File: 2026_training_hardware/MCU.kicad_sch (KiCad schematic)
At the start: 2 parts, among them J1 RJ45_LED_Shielded, U1 Teensy4.1_DEV-16771

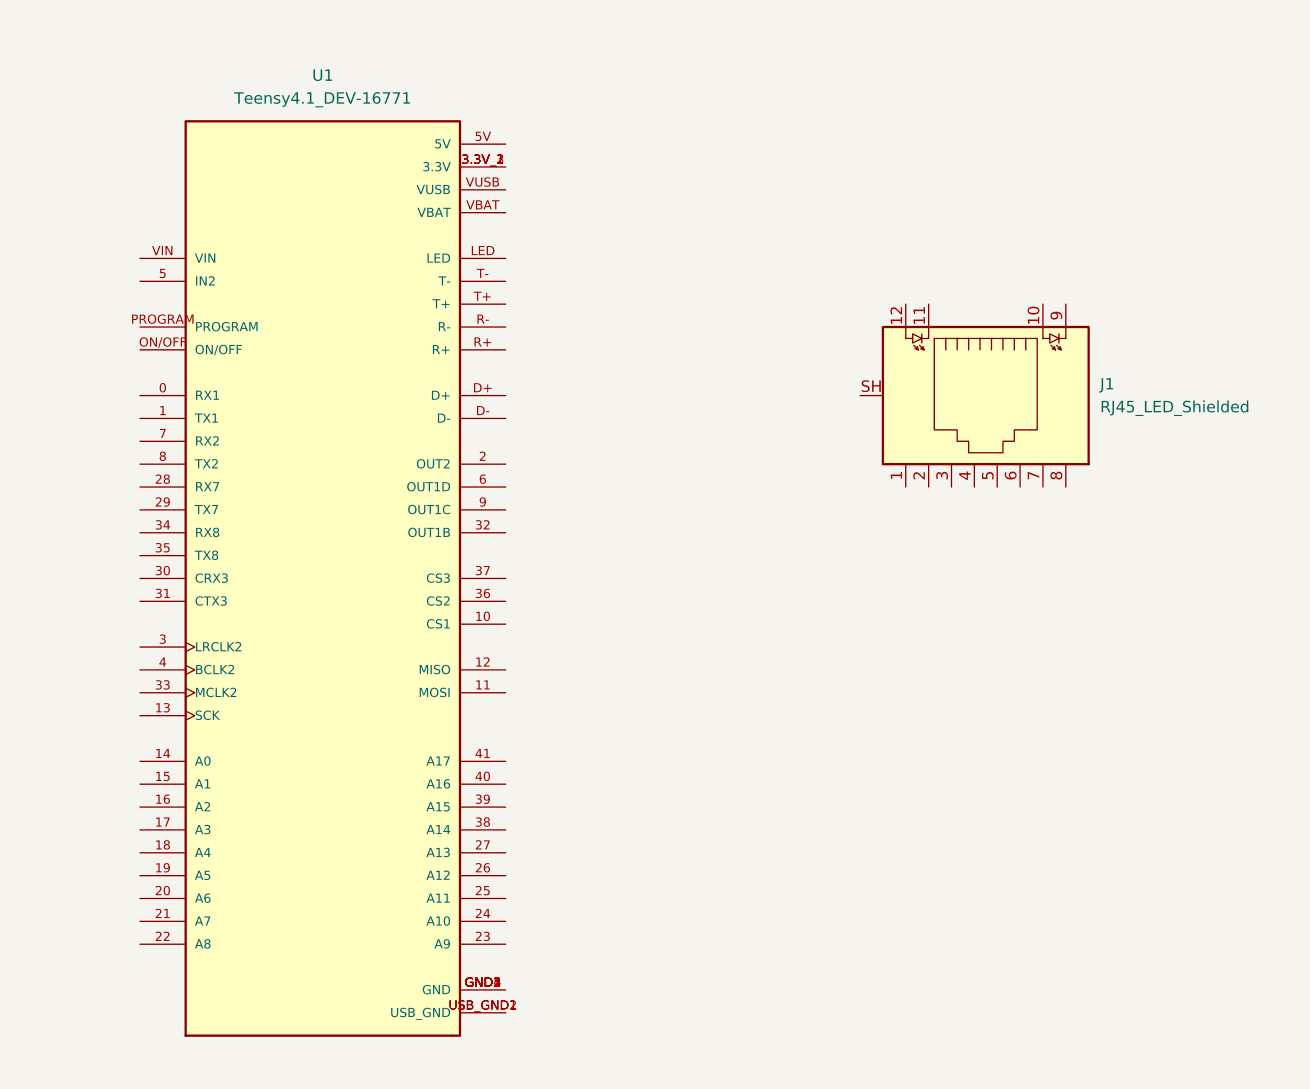
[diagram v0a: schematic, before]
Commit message: Add Ethernet
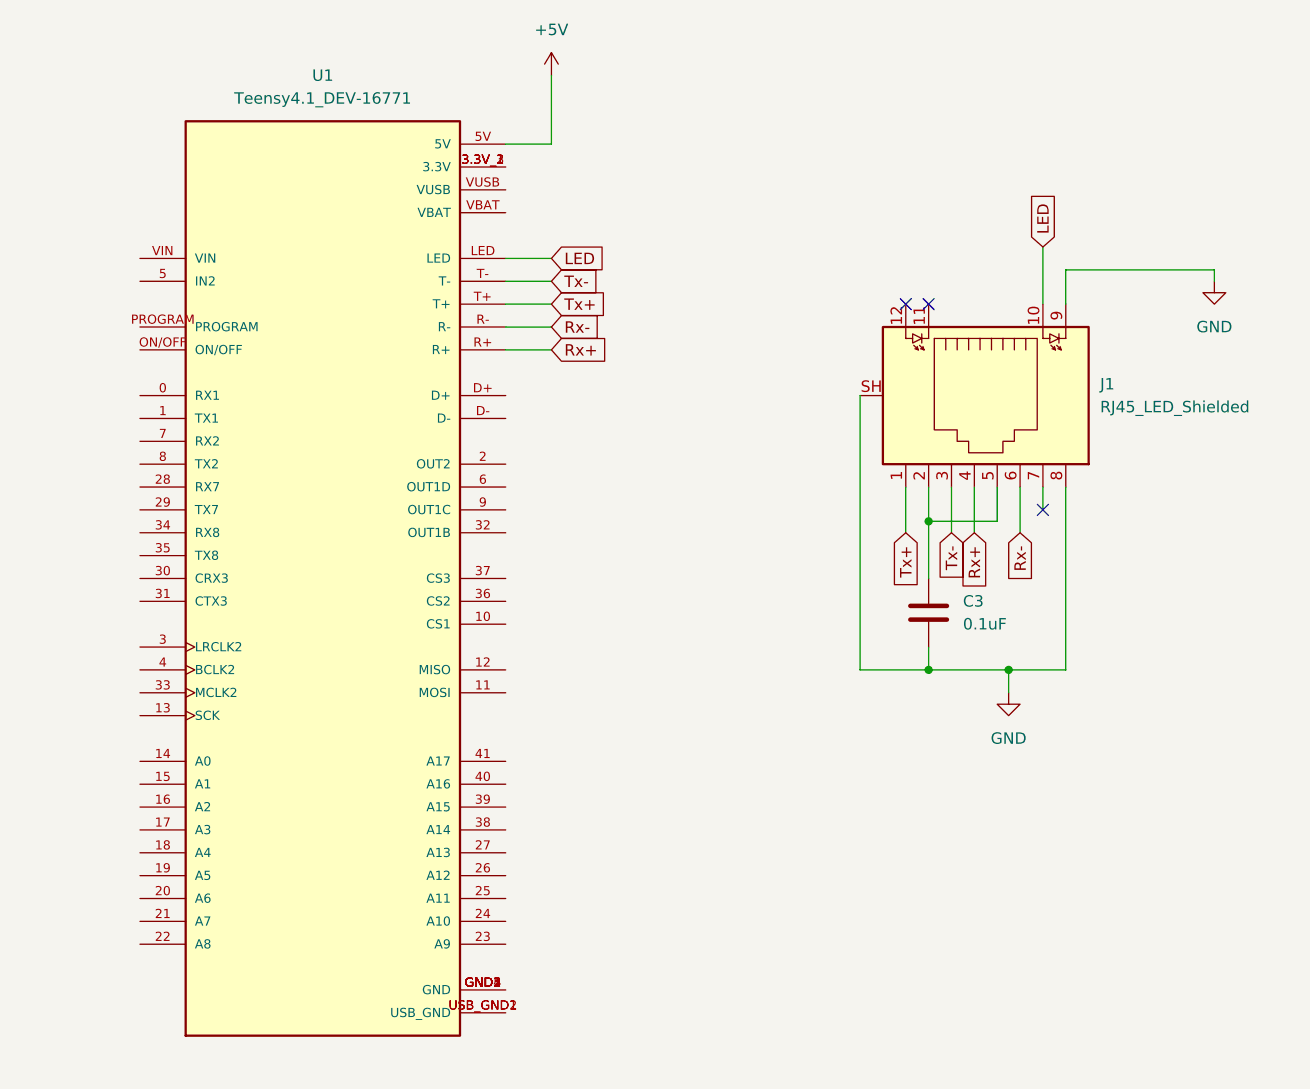
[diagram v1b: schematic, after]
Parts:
- added C3: 0.1uF, symbol Device:C
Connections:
- net +5V: now reaches U1.5V
- net LED: now reaches U1.LED
- net LED: now also J1.10
- net Rx+: now reaches U1.R+
- net Rx+: now also J1.4
- net Rx-: now reaches U1.R-
- net Rx-: now also J1.6
- net Tx+: now reaches U1.T+
- net Tx+: now also J1.1
- net Tx-: now reaches U1.T-
- net Tx-: now also J1.3
- net at J1.2: now also J1.5, C3.1
- net GND: now reaches J1.8
- net GND: now also J1.9, J1.SH, C3.2
- no-connect marks 0 -> 3

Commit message: Add CAN
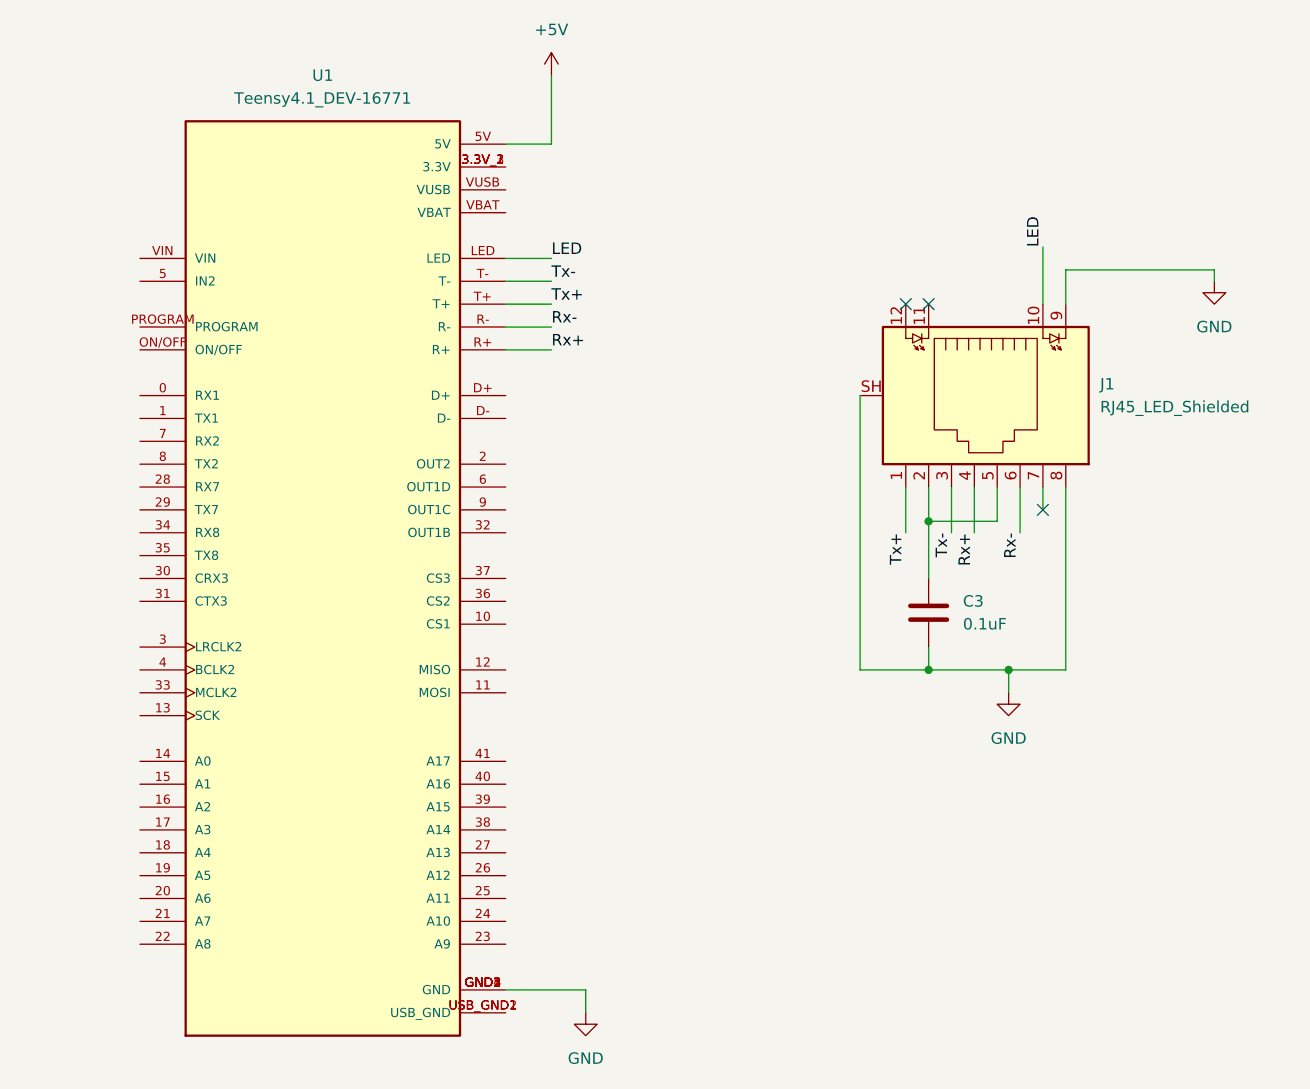
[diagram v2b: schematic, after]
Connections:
- net GND: now also U1.GND1 (GND), U1.GND2 (GND), U1.GND3 (GND), U1.GND4 (GND), U1.GND5 (GND)
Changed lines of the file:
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@@
+	(wire
+		(pts
+			(xy 111.76 143.51) (xy 111.76 146.05)
+		)
+		(stroke
+			(width 0)
+			(type default)
+		)
+	)
 	(wire
 		(pts
@@
 	(wire
 		(pts
+			(xy 102.87 143.51) (xy 111.76 143.51)
+		)
+		(stroke
+			(width 0)
+			(type default)
+		)
+	)
+	(wire
+		(pts
 			(xy 149.86 87.63) (xy 149.86 91.44)
 		)
@@
 		)
 	)
-	(global_label "Tx+"
-		(shape input)
-		(at 107.95 67.31 0)
-		(fields_autoplaced yes)
+	(label "Rx-"
+		(at 107.95 69.85 0)
 		(effects
 			(font
 				(size 1.27 1.27)
 			)
-			(justify left)
-		)
-		(property "Intersheetrefs" "${INTERSHEET_REFS}"
-			(at 114.5033 67.31 0)
-			(effects
-				(font
-					(size 1.27 1.27)
-				)
-				(justify left)
-				(hide yes)
-			)
-		)
-	)
-	(global_label "LED"
-		(shape input)
-		(at 107.95 62.23 0)
-		(fields_autoplaced yes)
+			(justify left bottom)
+		)
+	)
+	(label "Rx+"
+		(at 154.94 92.71 270)
 		(effects
 			(font
 				(size 1.27 1.27)
 			)
-			(justify left)
-		)
-		(property "Intersheetrefs" "${INTERSHEET_REFS}"
-			(at 114.3823 62.23 0)
-			(effects
-				(font
-					(size 1.27 1.27)
-				)
-				(justify left)
-				(hide yes)
-			)
-		)
-	)
-	(global_label "Rx-"
-		(shape input)
-		(at 160.02 92.71 270)
-		(fields_autoplaced yes)
+			(justify right bottom)
+		)
+	)
+	(label "Rx+"
+		(at 107.95 72.39 0)
 		(effects
 			(font
 				(size 1.27 1.27)
 			)
-			(justify right)
-		)
-		(property "Intersheetrefs" "${INTERSHEET_REFS}"
-			(at 160.02 99.5657 90)
-			(effects
-				(font
-					(size 1.27 1.27)
-				)
-				(justify right)
-				(hide yes)
-			)
-		)
-	)
-	(global_label "Tx+"
-		(shape input)
-		(at 147.32 92.71 270)
-		(fields_autoplaced yes)
+			(justify left bottom)
+		)
+	)
+	(label "Tx-"
+		(at 107.95 64.77 0)
 		(effects
 			(font
 				(size 1.27 1.27)
 			)
-			(justify right)
-		)
-		(property "Intersheetrefs" "${INTERSHEET_REFS}"
-			(at 147.32 99.2633 90)
-			(effects
-				(font
-					(size 1.27 1.27)
-				)
-				(justify right)
-				(hide yes)
-			)
-		)
-	)
-	(global_label "Rx+"
-		(shape input)
-		(at 154.94 92.71 270)
-		(fields_autoplaced yes)
+			(justify left bottom)
+		)
+	)
+	(label "Rx-"
+		(at 160.02 92.71 270)
 		(effects
 			(font
 				(size 1.27 1.27)
 			)
-			(justify right)
-		)
-		(property "Intersheetrefs" "${INTERSHEET_REFS}"
-			(at 154.94 99.5657 90)
-			(effects
-				(font
-					(size 1.27 1.27)
-				)
-				(justify right)
-				(hide yes)
-			)
-		)
-	)
-	(global_label "Rx-"
-		(shape input)
-		(at 107.95 69.85 0)
-		(fields_autoplaced yes)
+			(justify right bottom)
+		)
+	)
+	(label "Tx-"
+		(at 152.4 92.71 270)
 		(effects
 			(font
 				(size 1.27 1.27)
 			)
-			(justify left)
-		)
-		(property "Intersheetrefs" "${INTERSHEET_REFS}"
-			(at 114.8057 69.85 0)
-			(effects
-				(font
-					(size 1.27 1.27)
-				)
-				(justify left)
-				(hide yes)
-			)
-		)
-	)
-	(global_label "LED"
-		(shape input)
-		(at 162.56 60.96 90)
-		(fields_autoplaced yes)
+			(justify right bottom)
+		)
+	)
+	(label "Tx+"
+		(at 147.32 92.71 270)
 		(effects
 			(font
 				(size 1.27 1.27)
 			)
-			(justify left)
-		)
-		(property "Intersheetrefs" "${INTERSHEET_REFS}"
-			(at 162.56 54.5277 90)
-			(effects
-				(font
-					(size 1.27 1.27)
-				)
-				(justify left)
-				(hide yes)
-			)
-		)
-	)
-	(global_label "Rx+"
-		(shape input)
-		(at 107.95 72.39 0)
-		(fields_autoplaced yes)
+			(justify right bottom)
+		)
+	)
+	(label "Tx+"
+		(at 107.95 67.31 0)
 		(effects
 			(font
 				(size 1.27 1.27)
 			)
-			(justify left)
-		)
-		(property "Intersheetrefs" "${INTERSHEET_REFS}"
-			(at 114.8057 72.39 0)
-			(effects
-				(font
-					(size 1.27 1.27)
-				)
-				(justify left)
-				(hide yes)
-			)
-		)
-	)
-	(global_label "Tx-"
-		(shape input)
-		(at 107.95 64.77 0)
-		(fields_autoplaced yes)
+			(justify left bottom)
+		)
+	)
+	(label "LED"
+		(at 162.56 60.96 90)
 		(effects
 			(font
 				(size 1.27 1.27)
 			)
-			(justify left)
-		)
-		(property "Intersheetrefs" "${INTERSHEET_REFS}"
-			(at 114.5033 64.77 0)
-			(effects
-				(font
-					(size 1.27 1.27)
-				)
-				(justify left)
-				(hide yes)
-			)
-		)
-	)
-	(global_label "Tx-"
-		(shape input)
-		(at 152.4 92.71 270)
-		(fields_autoplaced yes)
+			(justify left bottom)
+		)
+	)
+	(label "LED"
+		(at 107.95 62.23 0)
 		(effects
 			(font
 				(size 1.27 1.27)
 			)
-			(justify right)
-		)
-		(property "Intersheetrefs" "${INTERSHEET_REFS}"
-			(at 152.4 99.2633 90)
-			(effects
-				(font
-					(size 1.27 1.27)
-				)
-				(justify right)
-				(hide yes)
-			)
+			(justify left bottom)
 		)
 	)
@@
 					(unit 1)
 				)
+			)
+		)
+	)
+	(symbol
+		(lib_id "power:GND")
+		(at 111.76 146.05 0)
+		(unit 1)
+		(exclude_from_sim no)
+		(in_bom yes)
+		(on_board yes)
+		(dnp no)
+		(fields_autoplaced yes)
+		(property "Reference" "#PWR011"
+			(at 111.76 152.4 0)
+			(effects
+				(font
+					(size 1.27 1.27)
+				)
+				(hide yes)
+			)
+		)
+		(property "Value" "GND"
+			(at 111.76 151.13 0)
+			(effects
+				(font
+					(size 1.27 1.27)
+				)
+			)
+		)
+		(property "Footprint" ""
+			(at 111.76 146.05 0)
+			(effects
+				(font
+					(size 1.27 1.27)
+				)
+				(hide yes)
+			)
+		)
+		(property "Datasheet" ""
+			(at 111.76 146.05 0)
+			(effects
+				(font
+					(size 1.27 1.27)
+				)
+				(hide yes)
+			)
+		)
+		(property "Description" "Power symbol creates a global label with name \"GND\" , ground"
+			(at 111.76 146.05 0)
+			(effects
+				(font
+					(size 1.27 1.27)
+				)
+				(hide yes)
+			)
+		)
+		(pin "1"
+		)
+		(instances
+			(project ""
+				(path "/396efc46-0624-4b5a-8d52-10436ddb56f1/c7e42e04-9596-414a-b3e5-d4438426bcd6"
+					(reference "#PWR011")
+					(unit 1)
+				)

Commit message: Finish Schematic
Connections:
- net STBY: now reaches U1.2 (OUT2)
- net CTX1: now reaches U1.22 (A8)
- net CRX1: now reaches U1.23 (A9)
- net +3V3: now reaches U1.3.3V_1 (3.3V), U1.3.3V_2 (3.3V), U1.3.3V_3 (3.3V)
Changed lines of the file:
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@@
+	(wire
+		(pts
+			(xy 119.38 41.91) (xy 119.38 52.07)
+		)
+		(stroke
+			(width 0)
+			(type default)
+		)
+	)
 	(wire
 		(pts
@@
 	(wire
 		(pts
+			(xy 102.87 85.09) (xy 107.95 85.09)
+		)
+		(stroke
+			(width 0)
+			(type default)
+		)
+	)
+	(wire
+		(pts
 			(xy 162.56 60.96) (xy 162.56 67.31)
 		)
@@
 	(wire
 		(pts
+			(xy 55.88 138.43) (xy 62.23 138.43)
+		)
+		(stroke
+			(width 0)
+			(type default)
+		)
+	)
+	(wire
+		(pts
 			(xy 107.95 49.53) (xy 107.95 41.91)
 		)
@@
 	(wire
 		(pts
+			(xy 102.87 52.07) (xy 119.38 52.07)
+		)
+		(stroke
+			(width 0)
+			(type default)
+		)
+	)
+	(wire
+		(pts
 			(xy 181.61 63.5) (xy 181.61 64.77)
 		)
@@
 		(pts
 			(xy 102.87 49.53) (xy 107.95 49.53)
+		)
+		(stroke
+			(width 0)
+			(type default)
+		)
+	)
+	(wire
+		(pts
+			(xy 102.87 138.43) (xy 107.95 138.43)
 		)
 		(stroke
@@
 			)
 			(justify left bottom)
+		)
+	)
+	(hierarchical_label "CTX1"
+		(shape output)
+		(at 55.88 138.43 180)
+		(effects
+			(font
+				(size 1.27 1.27)
+			)
+			(justify right)
+		)
+	)
+	(hierarchical_label "STBY"
+		(shape output)
+		(at 107.95 85.09 0)
+		(effects
+			(font
+				(size 1.27 1.27)
+			)
+			(justify left)
+		)
+	)
+	(hierarchical_label "CRX1"
+		(shape input)
+		(at 107.95 138.43 0)
+		(effects
+			(font
+				(size 1.27 1.27)
+			)
+			(justify left)
 		)
 	)
@@
 					(unit 1)
 				)
+			)
+		)
+	)
+	(symbol
+		(lib_id "power:+3V3")
+		(at 119.38 41.91 0)
+		(unit 1)
+		(exclude_from_sim no)
+		(in_bom yes)
+		(on_board yes)
+		(dnp no)
+		(fields_autoplaced yes)
+		(property "Reference" "#PWR014"
+			(at 119.38 45.72 0)
+			(effects
+				(font
+					(size 1.27 1.27)
+				)
+				(hide yes)
+			)
+		)
+		(property "Value" "+3V3"
+			(at 119.38 36.83 0)
+			(effects
+				(font
+					(size 1.27 1.27)
+				)
+			)
+		)
+		(property "Footprint" ""
+			(at 119.38 41.91 0)
+			(effects
+				(font
+					(size 1.27 1.27)
+				)
+				(hide yes)
+			)
+		)
+		(property "Datasheet" ""
+			(at 119.38 41.91 0)
+			(effects
+				(font
+					(size 1.27 1.27)
+				)
+				(hide yes)
+			)
+		)
+		(property "Description" "Power symbol creates a global label with name \"+3V3\""
+			(at 119.38 41.91 0)
+			(effects
+				(font
+					(size 1.27 1.27)
+				)
+				(hide yes)
+			)
+		)
+		(pin "1"
+		)
+		(instances
+			(project ""
+				(path "/396efc46-0624-4b5a-8d52-10436ddb56f1/c7e42e04-9596-414a-b3e5-d4438426bcd6"
+					(reference "#PWR014")
+					(unit 1)
+				)
